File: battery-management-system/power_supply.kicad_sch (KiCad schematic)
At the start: 24 parts, among them J14 SUPPLY, U1 L6982C33DR, U2 L6982C33DR

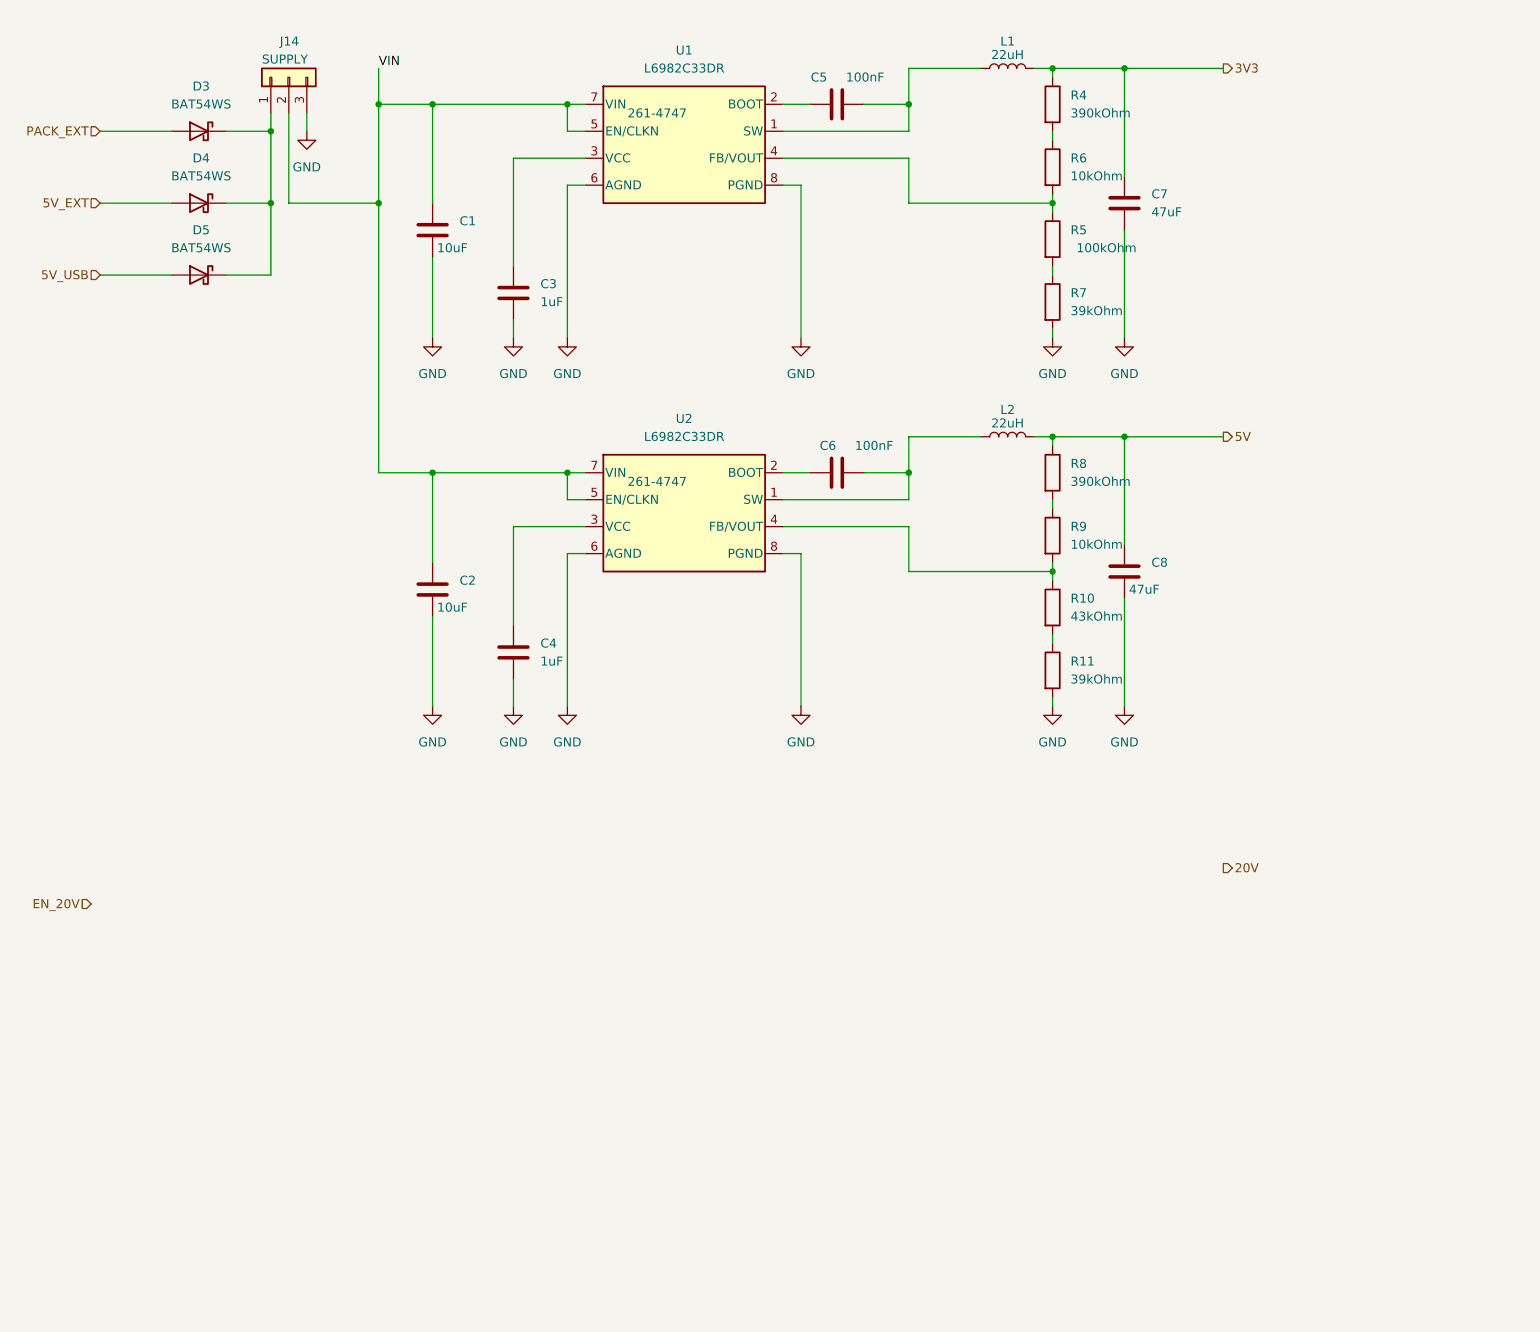
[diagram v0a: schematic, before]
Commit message: add 20V supply
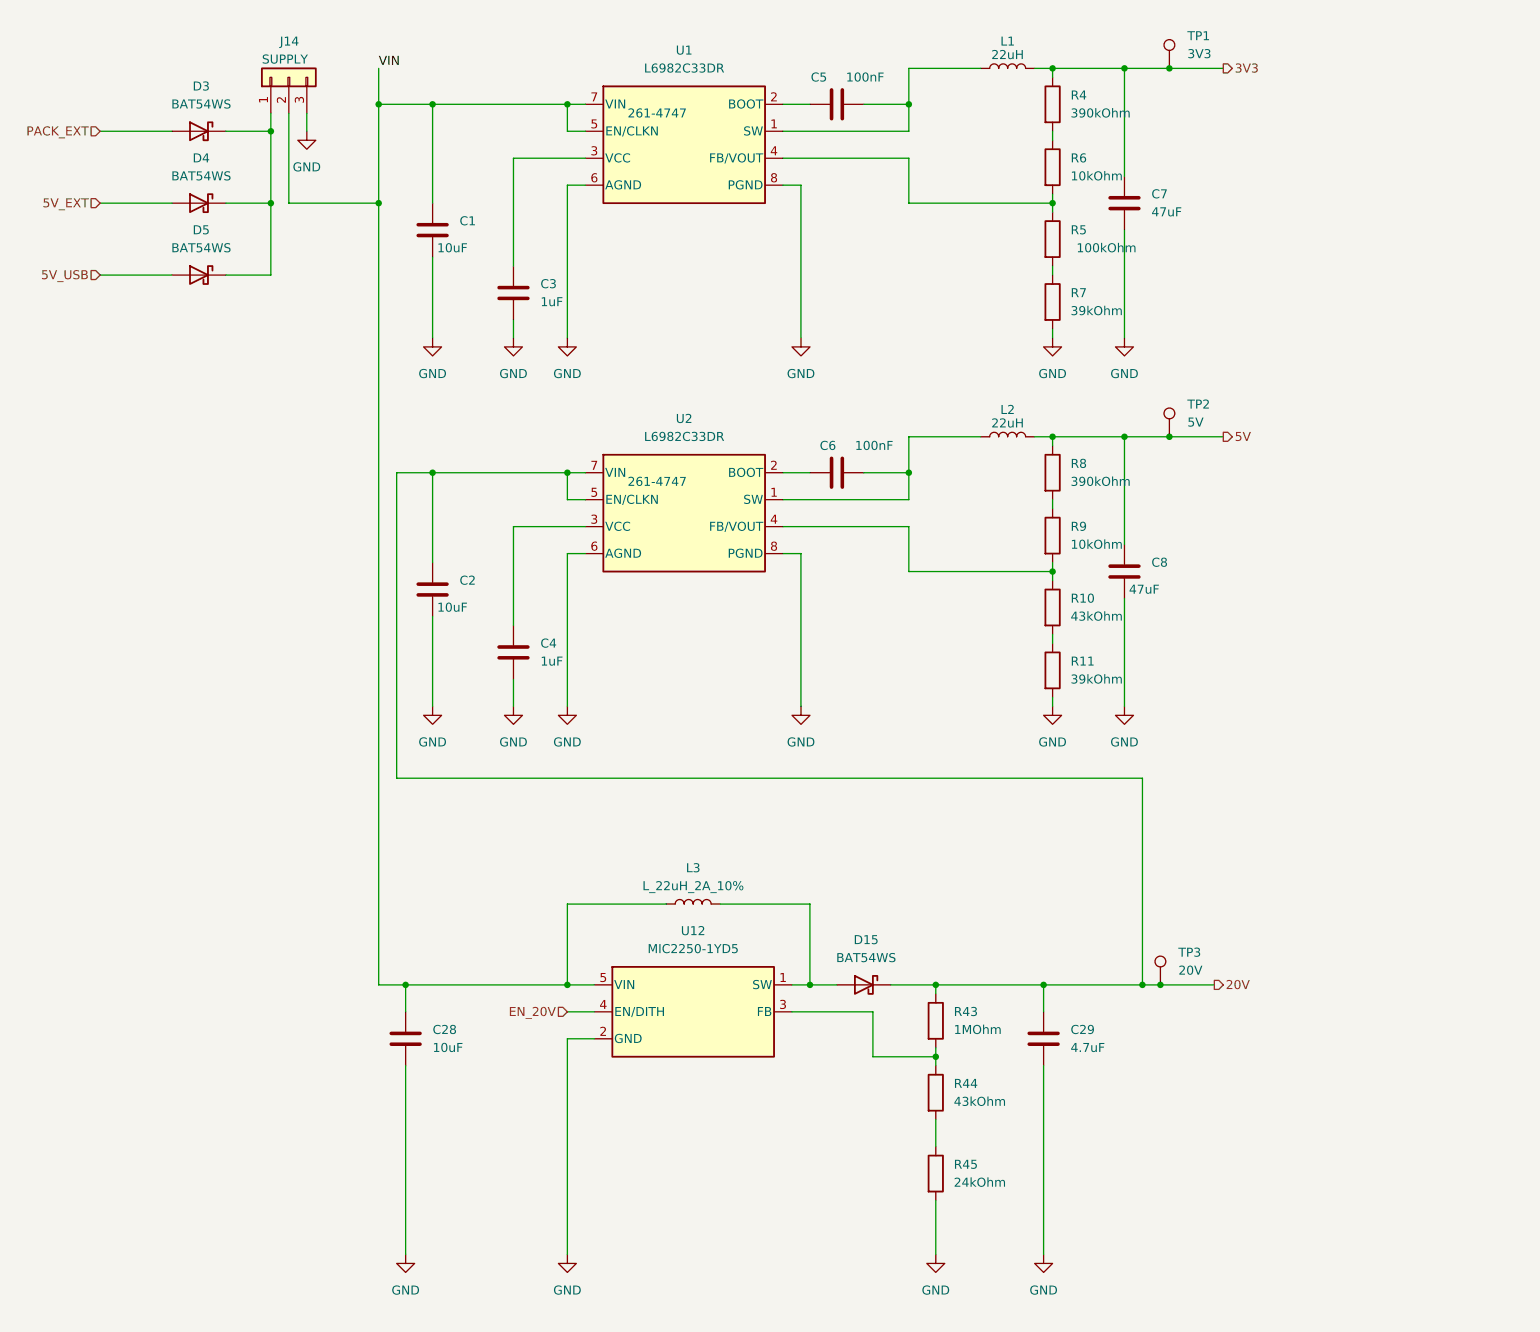
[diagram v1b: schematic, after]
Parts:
- added C28: 10uF, benediktibk:C_1210_3225Metric_Pad1.33x2.70mm_HandSolder, symbol benediktibk:C_10uF_SMD_1210_50V_20%
- added C29: 4.7uF, benediktibk:C_0805_2012Metric_Pad1.18x1.45mm_HandSolder, symbol benediktibk:C_4_7uF_SMD_0805_50V_10%
- added D15: BAT54WS, benediktibk:D_SOD-323, symbol benediktibk:BAT54WS
- added L3: L_22uH_2A_10%, benediktibk:L_Radial_D9.5mm_P5.00mm_Fastron_07HVP, symbol benediktibk:L_22uH_2A_10%
- added R43: 1MOhm, benediktibk:R_0603_1608Metric_Pad0.98x0.95mm_HandSolder, symbol benediktibk:R_1MOhm_SMD_0603_100mW_1%
- added R44: 43kOhm, benediktibk:R_0603_1608Metric_Pad0.98x0.95mm_HandSolder, symbol benediktibk:R_43kOhm_SMD_0603_100mW_1%
- added R45: 24kOhm, benediktibk:R_0603_1608Metric_Pad0.98x0.95mm_HandSolder, symbol benediktibk:R_24kOhm_SMD_0603_100mW_1%
- added TP1: 3V3, benediktibk:TestPoint_Pad_D2.0mm, symbol benediktibk:TestPoint_2_0mm
- added TP2: 5V, benediktibk:TestPoint_Pad_D2.0mm, symbol benediktibk:TestPoint_2_0mm
- added TP3: 20V, benediktibk:TestPoint_Pad_D2.0mm, symbol benediktibk:TestPoint_2_0mm
- added U12: MIC2250-1YD5, benediktibk:SOT-23-5, symbol benediktibk:MIC2250-1YD5
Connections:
- net 20V: now also C2.1, U2.5 (EN/CLKN), U2.7 (VIN), C29.1, D15.1 (K), R43.1, TP3.1
- net 3V3: now also TP1.1
- net 5V: now also TP2.1
- net EN_20V: now also U12.4 (EN/DITH)
- net GND: now also C28.2, C29.2, R45.2, U12.2 (GND)
- net VIN: now also C28.1, L3.1, U12.5 (VIN); no longer C2.1, U2.5 (EN/CLKN), U2.7 (VIN)
- new net: R43.2, R44.1, U12.3 (FB)
- new net: R44.2, R45.1
- new net: D15.2 (A), L3.2, U12.1 (SW)

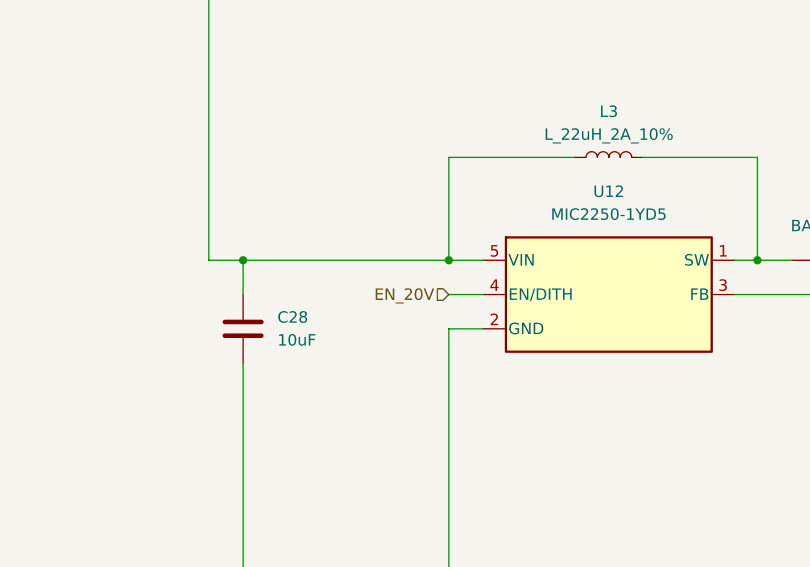
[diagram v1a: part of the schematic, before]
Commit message: add balancing sheet
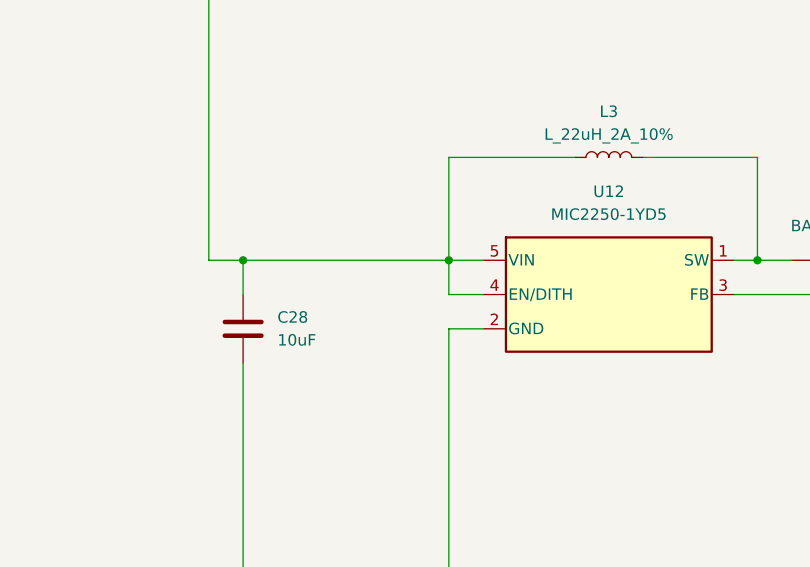
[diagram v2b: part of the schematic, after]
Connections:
- net EN_20V is gone; now on net VIN: U12.4 (EN/DITH)
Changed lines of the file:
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@@
+    (stroke (width 0) (type default))
+  )
+  (wire (pts (xy 93.98 149.86) (xy 93.98 153.67))
     (stroke (width 0) (type default))
   )
@@
     (effects (font (size 1.27 1.27)) (justify left))
   )
-  (hierarchical_label "EN_20V" (shape input) (at 93.98 153.67 180) (fields_autoplaced)
-    (effects (font (size 1.27 1.27)) (justify right))
-  )
   (symbol (lib_id "benediktibk:R_10kOhm_SMD_0603_100mW_1%") (at 162.56 86.36 0) (unit 1)

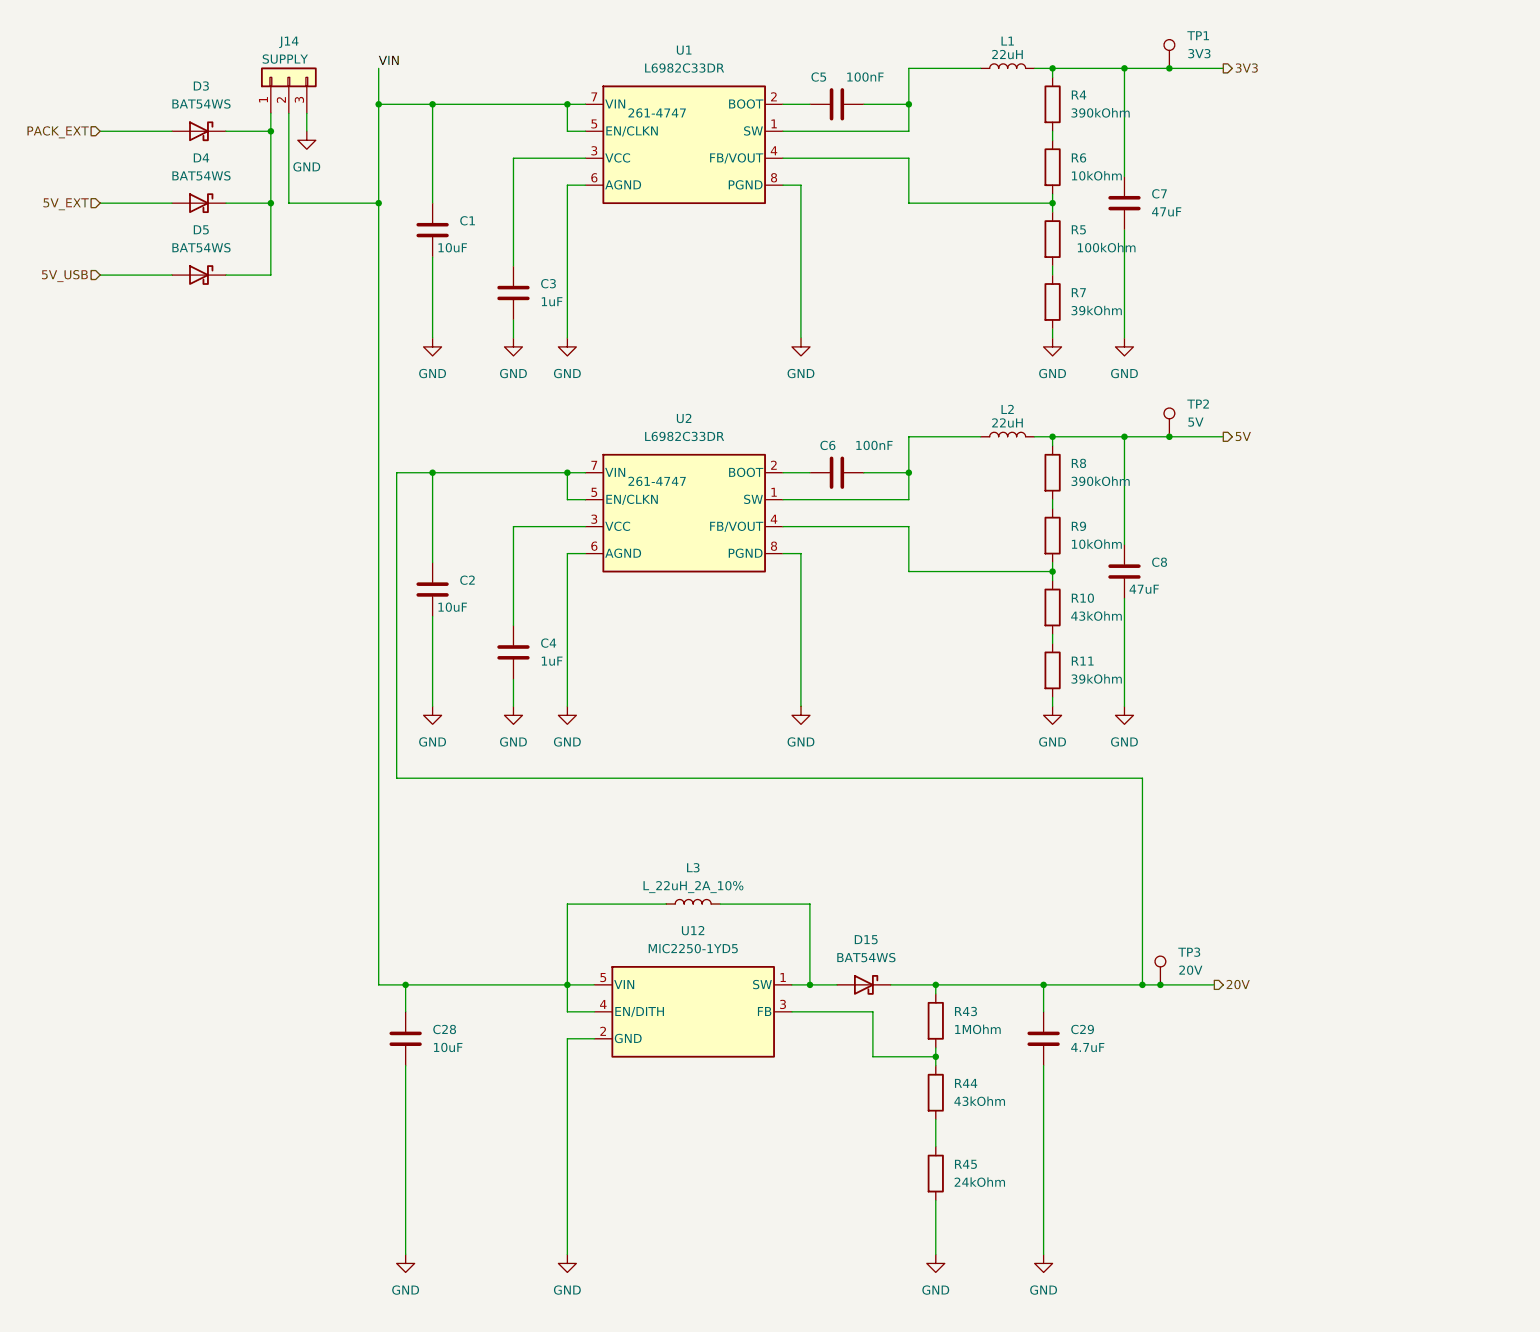
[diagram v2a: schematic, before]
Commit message: add fuel gauge IC
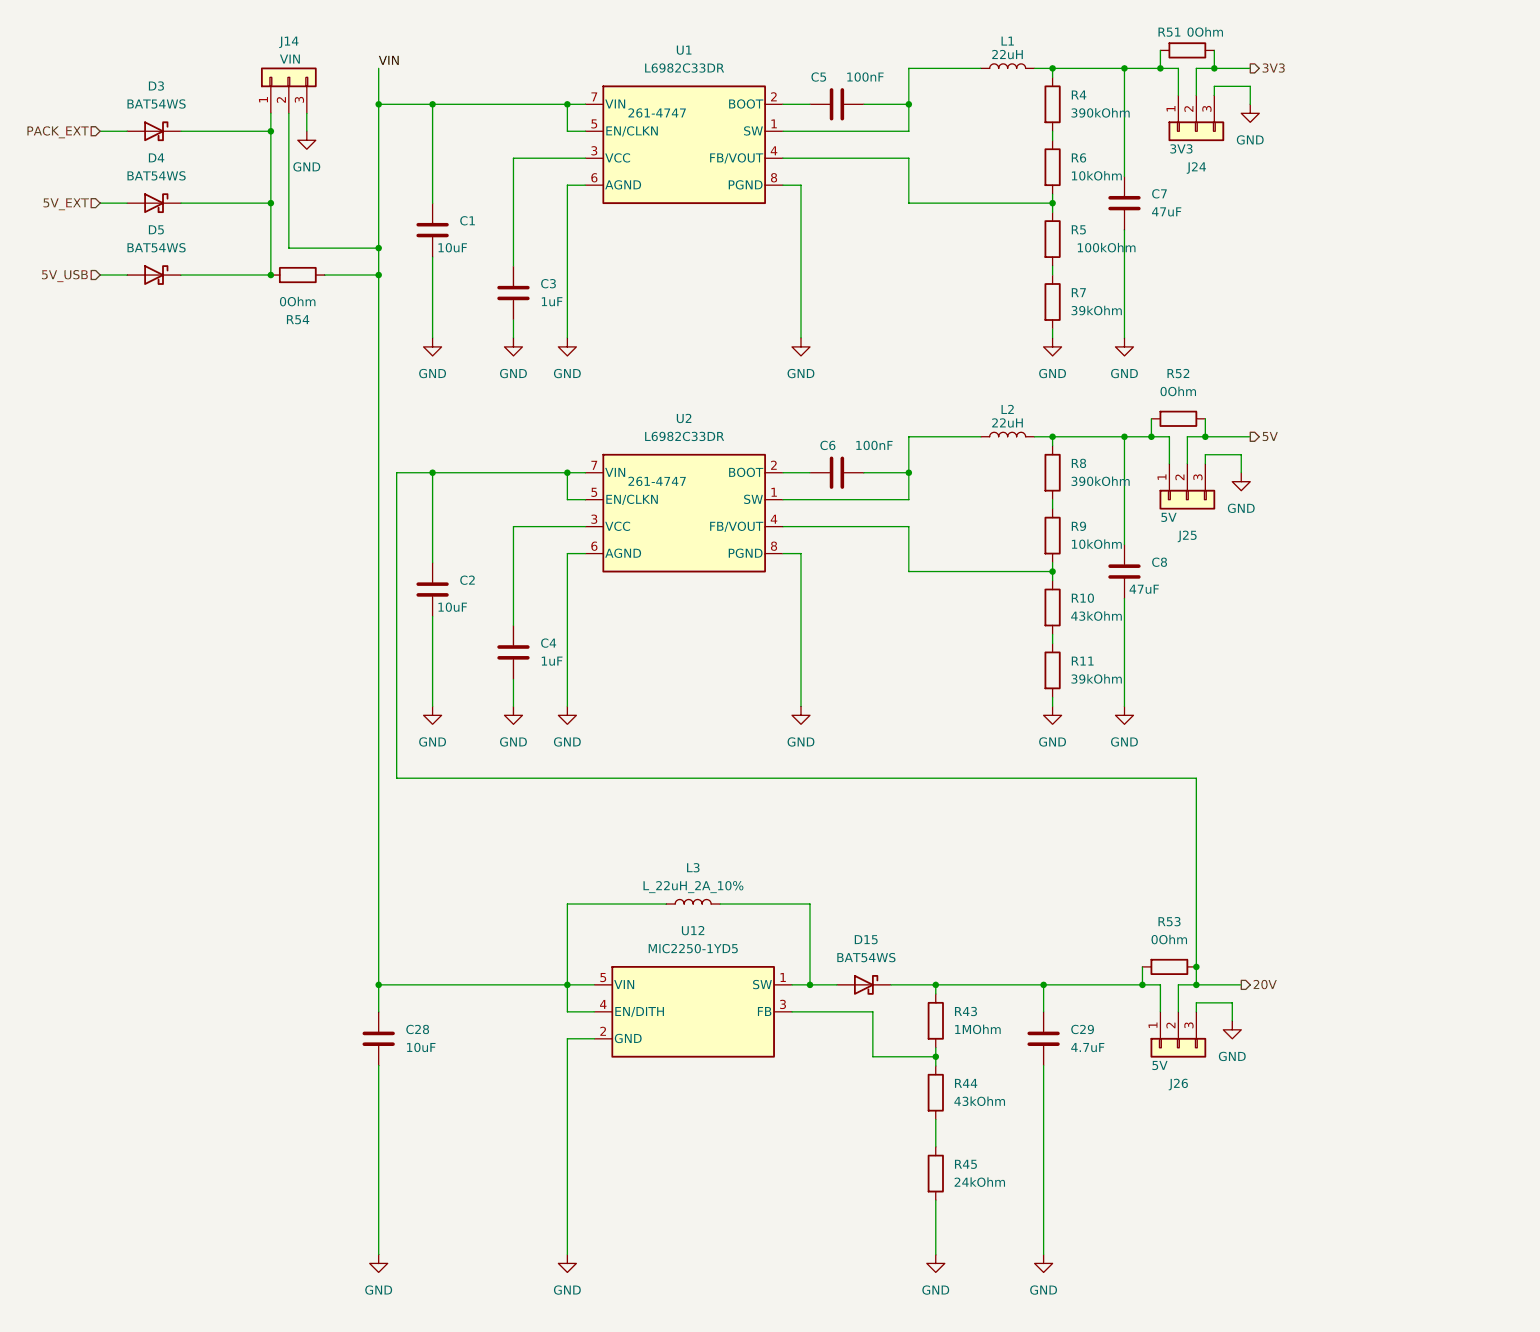
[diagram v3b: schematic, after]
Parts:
- removed TP1: 3V3, benediktibk:TestPoint_Pad_D2.0mm, symbol benediktibk:TestPoint_2_0mm
- removed TP2: 5V, benediktibk:TestPoint_Pad_D2.0mm, symbol benediktibk:TestPoint_2_0mm
- removed TP3: 20V, benediktibk:TestPoint_Pad_D2.0mm, symbol benediktibk:TestPoint_2_0mm
- added J24: 3V3, benediktibk:PinHeader_1x03_P2.54mm_Vertical, symbol benediktibk:Conn_01x03
- added J25, J26: 5V, benediktibk:PinHeader_1x03_P2.54mm_Vertical, symbol benediktibk:Conn_01x03
- added R51, R52, R53, R54: 0Ohm, benediktibk:R_0603_1608Metric_Pad0.98x0.95mm_HandSolder, symbol benediktibk:R_0Ohm_SMD_0603_100mW_0%
- J14: value SUPPLY -> VIN
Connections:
- net 20V: now also J26.2 (Pin_2), R53.1; no longer C29.1, D15.1 (K), R43.1
- net 3V3: now also J24.2 (Pin_2), R51.1; no longer C7.1, L1.1, R4.1
- net 5V: now also J25.2 (Pin_2), R52.1; no longer C8.1, L2.1, R8.1
- net GND: now also J24.3 (Pin_3), J25.3 (Pin_3), J26.3 (Pin_3)
- net VIN: now also R54.1
- net at D3.1 (K), D4.1 (K), D5.1 (K)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: now also R54.2
- new net: C7.1, J24.1 (Pin_1), L1.1, R4.1, R51.2
- new net: C8.1, J25.1 (Pin_1), L2.1, R52.2, R8.1
- new net: C29.1, D15.1 (K), J26.1 (Pin_1), R43.1, R53.2
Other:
- moved on the sheet: C28, D3, D4, D5
